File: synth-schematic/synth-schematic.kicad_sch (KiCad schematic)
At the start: 19 parts, among them U3 MCP4725xxx-xCH, U4 TL072

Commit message: Small fix
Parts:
- C(ceramic)1: footprint (none) -> Capacitor_SMD:C_3640_9110Metric
- C(electrolytic)1: footprint (none) -> Capacitor_SMD:CP_Elec_3x5.3
- C(tantalum)1: footprint (none) -> Capacitor_Tantalum_SMD:CP_EIA-1608-08_AVX-J
- LS2: footprint (none) -> Crystal:Crystal_SMD_3225-4Pin_3.2x2.5mm
- R1, R2, R3, R4: footprint (none) -> Resistor_SMD:R_0201_0603Metric
- RV1, RV2, RV3, RV4: footprint (none) -> Potentiometer_THT:Potentiometer_Piher_PT-15-H01_Horizontal
- SW1, SW2, SW3, SW4: footprint (none) -> Button_Switch_SMD:SW_Push_1P1T_NO_CK_PTS125Sx43PSMTR
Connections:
- net +5V: now also A2.5 (+5V)
- net GND: now also A2.29 (GND), A2.6 (GND), A2.7 (GND)
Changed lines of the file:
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@@
+	)
+	(junction
+		(at 151.13 83.82)
+		(diameter 0)
+		(color 0 0 0 0)
+	)
+	(junction
+		(at 153.67 83.82)
+		(diameter 0)
+		(color 0 0 0 0)
 	)
 	(junction
@@
 	(wire
 		(pts
+			(xy 151.13 83.82) (xy 153.67 83.82)
+		)
+		(stroke
+			(width 0)
+			(type default)
+		)
+	)
+	(wire
+		(pts
 			(xy 175.26 63.5) (xy 175.26 68.58)
 		)
@@
 	(wire
 		(pts
+			(xy 148.59 83.82) (xy 148.59 82.55)
+		)
+		(stroke
+			(width 0)
+			(type default)
+		)
+	)
+	(wire
+		(pts
 			(xy 123.19 86.36) (xy 123.19 88.9)
 		)
@@
 	(wire
 		(pts
+			(xy 148.59 82.55) (xy 146.05 82.55)
+		)
+		(stroke
+			(width 0)
+			(type default)
+		)
+	)
+	(wire
+		(pts
 			(xy 172.72 48.26) (xy 175.26 48.26)
 		)
@@
 	(wire
 		(pts
+			(xy 153.67 83.82) (xy 156.21 83.82)
+		)
+		(stroke
+			(width 0)
+			(type default)
+		)
+	)
+	(wire
+		(pts
 			(xy 191.77 104.14) (xy 193.04 104.14)
 		)
@@
 		(pts
 			(xy 196.85 87.63) (xy 196.85 93.98)
+		)
+		(stroke
+			(width 0)
+			(type default)
+		)
+	)
+	(wire
+		(pts
+			(xy 151.13 83.82) (xy 148.59 83.82)
 		)
 		(stroke
@@
 			)
 		)
-		(property "Footprint" ""
+		(property "Footprint" "Resistor_SMD:R_0201_0603Metric"
 			(at 120.65 44.45 0)
 			(effects
@@
 			)
 		)
-		(property "Footprint" ""
+		(property "Footprint" "Resistor_SMD:R_0201_0603Metric"
 			(at 120.65 58.42 0)
 			(effects
@@
 			)
 		)
-		(property "Footprint" ""
+		(property "Footprint" "Resistor_SMD:R_0201_0603Metric"
 			(at 120.65 86.36 0)
 			(effects
@@
 			)
 		)
-		(property "Footprint" ""
+		(property "Footprint" "Button_Switch_SMD:SW_Push_1P1T_NO_CK_PTS125Sx43PSMTR"
 			(at 128.27 80.01 0)
 			(effects
@@
 			)
 		)
-		(property "Footprint" ""
+		(property "Footprint" "Potentiometer_THT:Potentiometer_Piher_PT-15-H01_Horizontal"
 			(at 179.07 68.58 0)
 			(effects
@@
 			)
 		)
-		(property "Footprint" ""
+		(property "Footprint" "Potentiometer_THT:Potentiometer_Piher_PT-15-H01_Horizontal"
 			(at 179.07 48.26 0)
 			(effects
@@
 			)
 		)
-		(property "Footprint" ""
+		(property "Footprint" "Crystal:Crystal_SMD_3225-4Pin_3.2x2.5mm"
 			(at 207.01 109.22 0)
 			(effects
@@
 			)
 		)
-		(property "Footprint" ""
+		(property "Footprint" "Button_Switch_SMD:SW_Push_1P1T_NO_CK_PTS125Sx43PSMTR"
 			(at 128.27 66.04 0)
 			(effects
@@
 			)
 		)
-		(property "Footprint" ""
+		(property "Footprint" "Capacitor_Tantalum_SMD:CP_EIA-1608-08_AVX-J"
 			(at 189.23 94.9452 0)
 			(effects
@@
 				(path "/9aa8095e-6209-4c5d-96fa-dbe543a570c8"
 					(reference "C(tantalum)1")
+					(unit 1)
+				)
+			)
+		)
+	)
+	(symbol
+		(lib_id "power:GND")
+		(at 146.05 82.55 0)
+		(unit 1)
+		(exclude_from_sim no)
+		(in_bom yes)
+		(on_board yes)
+		(dnp no)
+		(fields_autoplaced yes)
+		(property "Reference" "#PWR03"
+			(at 146.05 88.9 0)
+			(effects
+				(font
+					(size 1.27 1.27)
+				)
+				(hide yes)
+			)
+		)
+		(property "Value" "GND"
+			(at 146.05 87.63 0)
+			(effects
+				(font
+					(size 1.27 1.27)
+				)
+			)
+		)
+		(property "Footprint" ""
+			(at 146.05 82.55 0)
+			(effects
+				(font
+					(size 1.27 1.27)
+				)
+				(hide yes)
+			)
+		)
+		(property "Datasheet" ""
+			(at 146.05 82.55 0)
+			(effects
+				(font
+					(size 1.27 1.27)
+				)
+				(hide yes)
+			)
+		)
+		(property "Description" "Power symbol creates a global label with name \"GND\" , ground"
+			(at 146.05 82.55 0)
+			(effects
+				(font
+					(size 1.27 1.27)
+				)
+				(hide yes)
+			)
+		)
+		(pin "1"
+		)
+		(instances
+			(project ""
+				(path "/9aa8095e-6209-4c5d-96fa-dbe543a570c8"
+					(reference "#PWR03")
 					(unit 1)
 				)
@@
 			)
 		)
-		(property "Footprint" ""
+		(property "Footprint" "Button_Switch_SMD:SW_Push_1P1T_NO_CK_PTS125Sx43PSMTR"
 			(at 128.27 93.98 0)
 			(effects
@@
 			)
 		)
-		(property "Footprint" ""
+		(property "Footprint" "Resistor_SMD:R_0201_0603Metric"
 			(at 120.65 72.39 0)
 			(effects
@@
 				(path "/9aa8095e-6209-4c5d-96fa-dbe543a570c8"
 					(reference "R3")
+					(unit 1)
+				)
+			)
+		)
+	)
+	(symbol
+		(lib_id "power:+5V")
+		(at 158.75 30.48 0)
+		(unit 1)
+		(exclude_from_sim no)
+		(in_bom yes)
+		(on_board yes)
+		(dnp no)
+		(fields_autoplaced yes)
+		(property "Reference" "#PWR02"
+			(at 158.75 34.29 0)
+			(effects
+				(font
+					(size 1.27 1.27)
+				)
+				(hide yes)
+			)
+		)
+		(property "Value" "+5V"
+			(at 158.75 25.4 0)
+			(effects
+				(font
+					(size 1.27 1.27)
+				)
+			)
+		)
+		(property "Footprint" ""
+			(at 158.75 30.48 0)
+			(effects
+				(font
+					(size 1.27 1.27)
+				)
+				(hide yes)
+			)
+		)
+		(property "Datasheet" ""
+			(at 158.75 30.48 0)
+			(effects
+				(font
+					(size 1.27 1.27)
+				)
+				(hide yes)
+			)
+		)
+		(property "Description" "Power symbol creates a global label with name \"+5V\""
+			(at 158.75 30.48 0)
+			(effects
+				(font
+					(size 1.27 1.27)
+				)
+				(hide yes)
+			)
+		)
+		(pin "1"
+		)
+		(instances
+			(project ""
+				(path "/9aa8095e-6209-4c5d-96fa-dbe543a570c8"
+					(reference "#PWR02")
 					(unit 1)
 				)
@@
 			)
 		)
-		(property "Footprint" ""
+		(property "Footprint" "Button_Switch_SMD:SW_Push_1P1T_NO_CK_PTS125Sx43PSMTR"
 			(at 128.27 52.07 0)
 			(effects
@@
 			)
 		)
-		(property "Footprint" ""
+		(property "Footprint" "Capacitor_SMD:C_3640_9110Metric"
 			(at 189.23 81.5848 0)
 			(effects
@@
 			)
 		)
-		(property "Footprint" ""
+		(property "Footprint" "Potentiometer_THT:Potentiometer_Piher_PT-15-H01_Horizontal"
 			(at 179.07 58.42 0)
 			(effects
@@
 			)
 		)
-		(property "Footprint" ""
+		(property "Footprint" "Capacitor_SMD:CP_Elec_3x5.3"
 			(at 200.66 103.1748 0)
 			(effects
@@
 			)
 		)
-		(property "Footprint" ""
+		(property "Footprint" "Potentiometer_THT:Potentiometer_Piher_PT-15-H01_Horizontal"
 			(at 179.07 38.1 0)
 			(effects

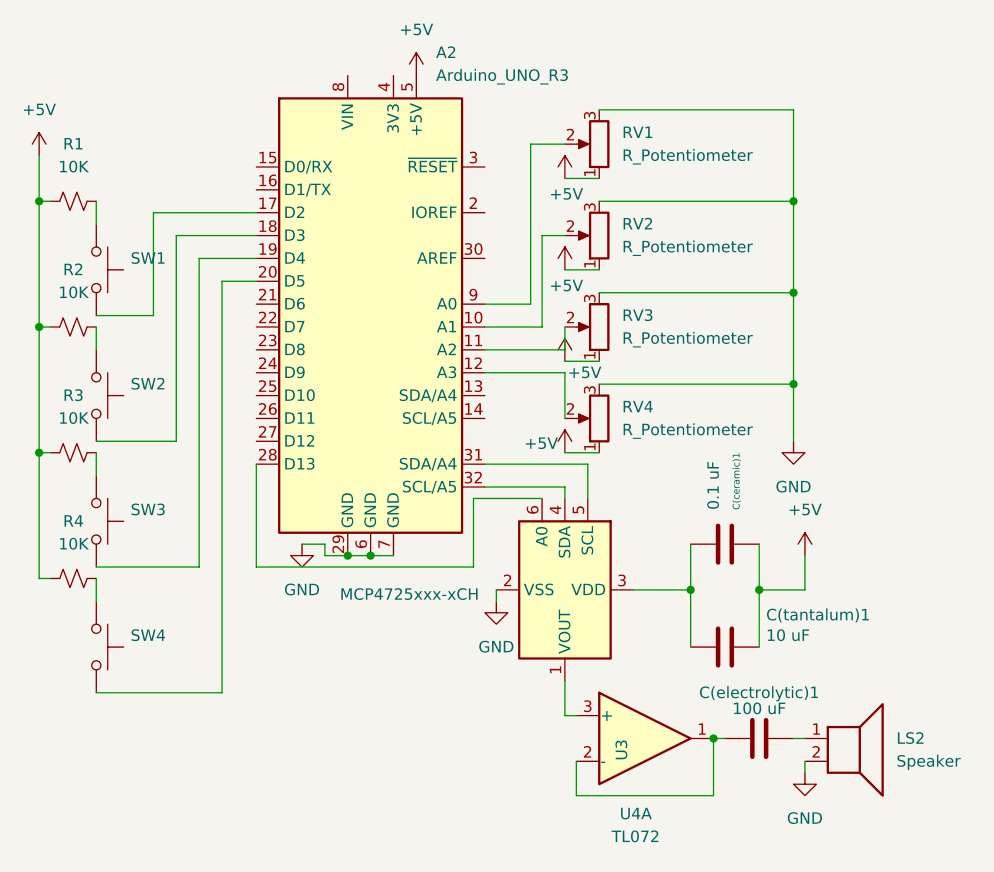
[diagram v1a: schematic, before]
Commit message: Updated schematic(no DAC allowed)
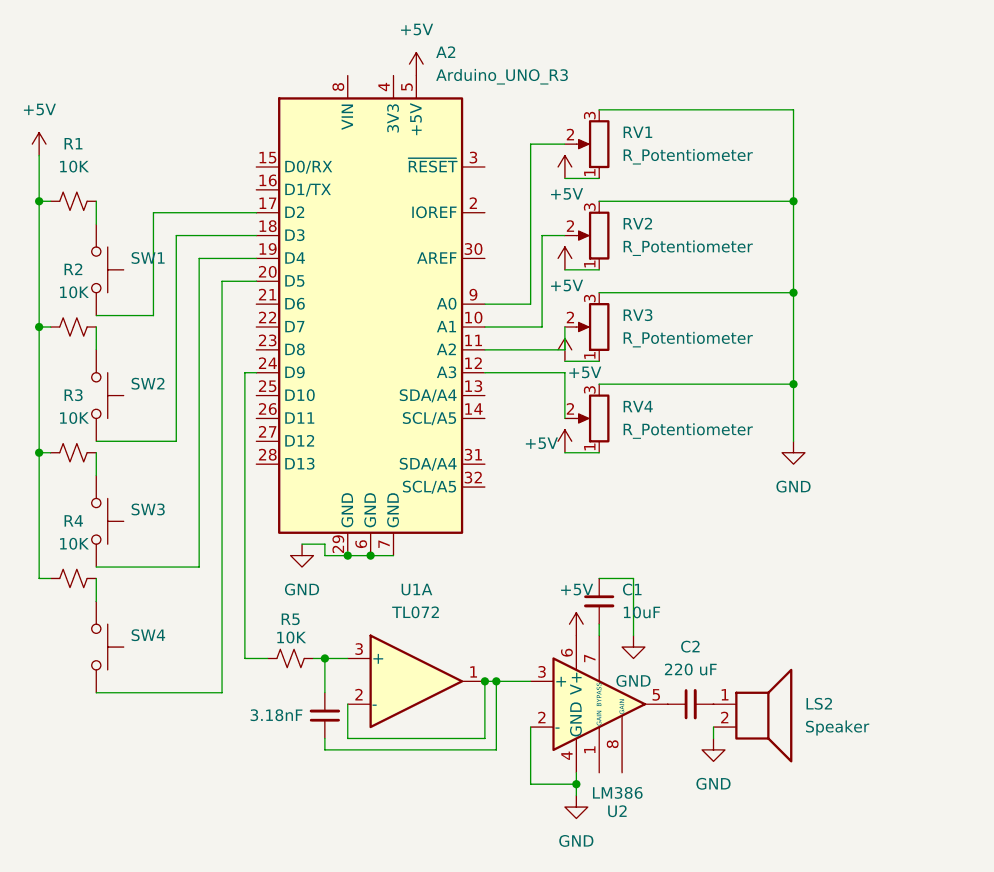
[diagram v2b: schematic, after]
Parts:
- removed C(ceramic)1: 0.1 uF, Capacitor_SMD:C_3640_9110Metric, symbol Device:C
- removed C(electrolytic)1: 100 uF, Capacitor_SMD:CP_Elec_3x5.3, symbol Device:C
- removed C(tantalum)1: 10 uF, Capacitor_Tantalum_SMD:CP_EIA-1608-08_AVX-J, symbol Device:C
- removed U3: MCP4725xxx-xCH, Package_TO_SOT_SMD:SOT-23-6, symbol Analog_DAC:MCP4725xxx-xCH
- removed U4: TL072, symbol Amplifier_Operational:TL072
- added C(ceramic): 3.18nF, symbol Device:C_Small
- added C1: 10uF, symbol Device:C_Small
- added C2: 220 uF, symbol Device:C_Small
- added R5: 10K, symbol Device:R_Small_US
- added U1: TL072, symbol Amplifier_Operational:TL072
- added U2: LM386, symbol Amplifier_Audio:LM386
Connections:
- net +5V: now also U2.6 (V+)
- net GND: now also C1.1, U2.2 (-), U2.4 (GND)
- net at LS2.1: now also C2.2
- net at A2.24 (D9): now also R5.1
- new net: C1.2, U2.7 (BYPASS)
- new net: C(ceramic).1, U1.1, U1.2 (-), U2.3 (+)
- new net: C2.1, U2.5
- new net: C(ceramic).2, R5.2, U1.3 (+)
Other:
- moved on the sheet: LS2

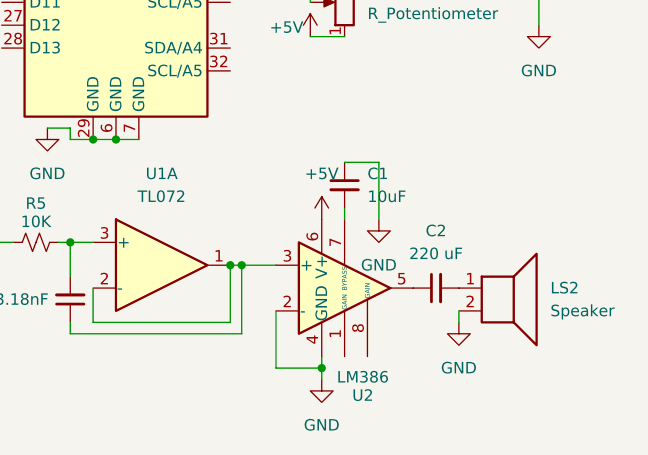
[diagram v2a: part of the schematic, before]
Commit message: base code for modulation
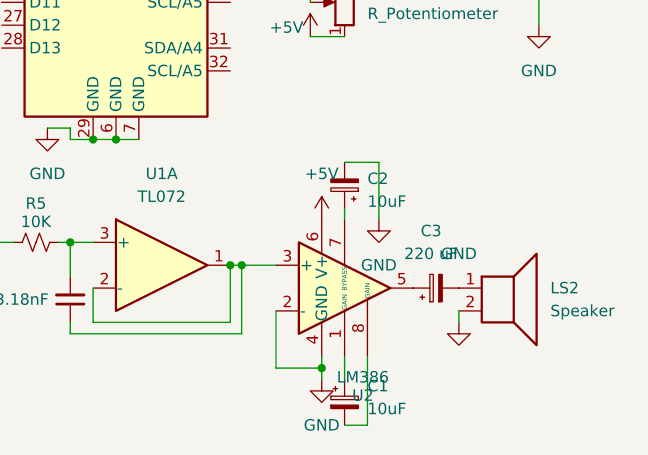
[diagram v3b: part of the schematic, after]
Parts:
- removed C1: 10uF, symbol Device:C_Small
- removed C2: 220 uF, symbol Device:C_Small
- added C1, C2: 10uF, symbol Device:C_Polarized_Small
- added C3: 220 uF, symbol Device:C_Polarized_Small
- renumbered C(ceramic) to C(ceramic)1
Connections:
- net GND: now also C2.2
- net at U2.7 (BYPASS): now also C2.1
- net at U2.1 (GAIN): now also C1.1
- net at U2.5: now also C3.1
- net at U2.8 (GAIN): now also C1.2
- net at LS2.1: now also C3.2
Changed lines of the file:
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@@
+	(wire
+		(pts
+			(xy 179.07 107.95) (xy 179.07 110.49)
+		)
+		(stroke
+			(width 0)
+			(type default)
+		)
+	)
 	(wire
 		(pts
@@
 	(wire
 		(pts
+			(xy 181.61 115.57) (xy 181.61 107.95)
+		)
+		(stroke
+			(width 0)
+			(type default)
+		)
+	)
+	(wire
+		(pts
 			(xy 171.45 38.1) (xy 175.26 38.1)
+		)
+		(stroke
+			(width 0)
+			(type default)
+		)
+	)
+	(wire
+		(pts
+			(xy 179.07 115.57) (xy 181.61 115.57)
 		)
 		(stroke
@@
 	)
 	(symbol
-		(lib_id "Device:C_Small")
-		(at 179.07 88.9 0)
-		(unit 1)
-		(exclude_from_sim no)
-		(in_bom yes)
-		(on_board yes)
-		(dnp no)
-		(fields_autoplaced yes)
-		(property "Reference" "C1"
-			(at 181.61 87.6362 0)
-			(effects
-				(font
-					(size 1.27 1.27)
-				)
-				(justify left)
-			)
-		)
-		(property "Value" "10uF"
-			(at 181.61 90.1762 0)
-			(effects
-				(font
-					(size 1.27 1.27)
-				)
-				(justify left)
-			)
-		)
-		(property "Footprint" ""
-			(at 179.07 88.9 0)
-			(effects
-				(font
-					(size 1.27 1.27)
-				)
-				(hide yes)
-			)
-		)
-		(property "Datasheet" "~"
-			(at 179.07 88.9 0)
-			(effects
-				(font
-					(size 1.27 1.27)
-				)
-				(hide yes)
-			)
-		)
-		(property "Description" "Unpolarized capacitor, small symbol"
-			(at 179.07 88.9 0)
-			(effects
-				(font
-					(size 1.27 1.27)
-				)
-				(hide yes)
-			)
-		)
-		(pin "1"
-		)
-		(pin "2"
-		)
-		(instances
-			(project ""
-				(path "/9aa8095e-6209-4c5d-96fa-dbe543a570c8"
-					(reference "C1")
-					(unit 1)
-				)
-			)
-		)
-	)
-	(symbol
 		(lib_id "Device:R_Small_US")
 		(at 120.65 58.42 90)
@@
 		(on_board yes)
 		(dnp no)
-		(fields_autoplaced yes)
 		(property "Reference" "#PWR012"
 			(at 191.77 110.49 0)
@@
 		)
 		(property "Value" "GND"
-			(at 191.77 109.22 0)
+			(at 191.77 96.52 0)
 			(effects
 				(font
@@
 	)
 	(symbol
+		(lib_id "Device:C_Polarized_Small")
+		(at 179.07 113.03 0)
+		(unit 1)
+		(exclude_from_sim no)
+		(in_bom yes)
+		(on_board yes)
+		(dnp no)
+		(fields_autoplaced yes)
+		(property "Reference" "C1"
+			(at 181.61 111.2138 0)
+			(effects
+				(font
+					(size 1.27 1.27)
+				)
+				(justify left)
+			)
+		)
+		(property "Value" "10uF"
+			(at 181.61 113.7538 0)
+			(effects
+				(font
+					(size 1.27 1.27)
+				)
+				(justify left)
+			)
+		)
+		(property "Footprint" ""
+			(at 179.07 113.03 0)
+			(effects
+				(font
+					(size 1.27 1.27)
+				)
+				(hide yes)
+			)
+		)
+		(property "Datasheet" "~"
+			(at 179.07 113.03 0)
+			(effects
+				(font
+					(size 1.27 1.27)
+				)
+				(hide yes)
+			)
+		)
+		(property "Description" "Polarized capacitor, small symbol"
+			(at 179.07 113.03 0)
+			(effects
+				(font
+					(size 1.27 1.27)
+				)
+				(hide yes)
+			)
+		)
+		(pin "1"
+		)
+		(pin "2"
+		)
+		(instances
+			(project ""
+				(path "/9aa8095e-6209-4c5d-96fa-dbe543a570c8"
+					(reference "C1")
+					(unit 1)
+				)
+			)
+		)
+	)
+	(symbol
 		(lib_id "Device:C_Small")
 		(at 148.59 101.6 180)
@@
 		(on_board yes)
 		(dnp no)
-		(property "Reference" "C(ceramic)"
+		(property "Reference" "C(ceramic)1"
 			(at 142.24 101.5937 90)
 			(effects
@@
 			(project ""
 				(path "/9aa8095e-6209-4c5d-96fa-dbe543a570c8"
-					(reference "C(ceramic)")
+					(reference "C(ceramic)1")
 					(unit 1)
 				)
@@
 	)
 	(symbol
+		(lib_id "Device:C_Polarized_Small")
+		(at 179.07 88.9 180)
+		(unit 1)
+		(exclude_from_sim no)
+		(in_bom yes)
+		(on_board yes)
+		(dnp no)
+		(fields_autoplaced yes)
+		(property "Reference" "C2"
+			(at 181.61 88.176 0)
+			(effects
+				(font
+					(size 1.27 1.27)
+				)
+				(justify right)
+			)
+		)
+		(property "Value" "10uF"
+			(at 181.61 90.716 0)
+			(effects
+				(font
+					(size 1.27 1.27)
+				)
+				(justify right)
+			)
+		)
+		(property "Footprint" ""
+			(at 179.07 88.9 0)
+			(effects
+				(font
+					(size 1.27 1.27)
+				)
+				(hide yes)
+			)
+		)
+		(property "Datasheet" "~"
+			(at 179.07 88.9 0)
+			(effects
+				(font
+					(size 1.27 1.27)
+				)
+				(hide yes)
+			)
+		)
+		(property "Description" "Polarized capacitor, small symbol"
+			(at 179.07 88.9 0)
+			(effects
+				(font
+					(size 1.27 1.27)
+				)
+				(hide yes)
+			)
+		)
+		(pin "2"
+		)
+		(pin "1"
+		)
+		(instances
+			(project ""
+				(path "/9aa8095e-6209-4c5d-96fa-dbe543a570c8"
+					(reference "C2")
+					(unit 1)
+				)
+			)
+		)
+	)
+	(symbol
 		(lib_id "power:+5V")
 		(at 176.53 92.71 0)
@@
 	)
 	(symbol
-		(lib_id "Device:C_Small")
-		(at 189.23 100.33 90)
-		(unit 1)
-		(exclude_from_sim no)
-		(in_bom yes)
-		(on_board yes)
-		(dnp no)
-		(fields_autoplaced yes)
-		(property "Reference" "C2"
-			(at 189.2363 93.98 90)
-			(effects
-				(font
-					(size 1.27 1.27)
-				)
-			)
-		)
-		(property "Value" "220 uF"
-			(at 189.2363 96.52 90)
-			(effects
-				(font
-					(size 1.27 1.27)
-				)
-			)
-		)
-		(property "Footprint" ""
-			(at 189.23 100.33 0)
-			(effects
-				(font
-					(size 1.27 1.27)
-				)
-				(hide yes)
-			)
-		)
-		(property "Datasheet" "~"
-			(at 189.23 100.33 0)
-			(effects
-				(font
-					(size 1.27 1.27)
-				)
-				(hide yes)
-			)
-		)
-		(property "Description" "Unpolarized capacitor, small symbol"
-			(at 189.23 100.33 0)
-			(effects
-				(font
-					(size 1.27 1.27)
-				)
-				(hide yes)
-			)
-		)
-		(pin "1"
-		)
-		(pin "2"
-		)
-		(instances
-			(project ""
-				(path "/9aa8095e-6209-4c5d-96fa-dbe543a570c8"
-					(reference "C2")
-					(unit 1)
-				)
-			)
-		)
-	)
-	(symbol
 		(lib_id "power:GND")
 		(at 200.66 71.12 0)
@@
 					(unit 1)
 				)
+			)
+		)
+	)
+	(symbol
+		(lib_id "Device:C_Polarized_Small")
+		(at 189.23 100.33 90)
+		(unit 1)
+		(exclude_from_sim no)
+		(in_bom yes)
+		(on_board yes)
+		(dnp no)
+		(fields_autoplaced yes)
+		(property "Reference" "C3"
+			(at 188.6839 93.98 90)
+			(effects
+				(font
+					(size 1.27 1.27)
+				)
+			)
+		)
+		(property "Value" "220 uF"
+			(at 188.6839 96.52 90)
+			(effects
+				(font
+					(size 1.27 1.27)
+				)
+			)
+		)
+		(property "Footprint" ""
+			(at 189.23 100.33 0)
+			(effects
+				(font
+					(size 1.27 1.27)
+				)
+				(hide yes)
+			)
+		)
+		(property "Datasheet" "~"
+			(at 189.23 100.33 0)
+			(effects
+				(font
+					(size 1.27 1.27)
+				)
+				(hide yes)
+			)
+		)
+		(property "Description" "Polarized capacitor, small symbol"
+			(at 189.23 100.33 0)
+			(effects
+				(font
+					(size 1.27 1.27)
+				)
+				(hide yes)
+			)
+		)
+		(pin "1"
+		)
+		(pin "2"
+		)
+		(instances
+			(project ""
+				(path "/9aa8095e-6209-4c5d-96fa-dbe543a570c8"
+					(reference "C3")
+					(unit 1)
+				)
